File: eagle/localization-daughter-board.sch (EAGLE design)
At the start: 22 parts, among them J1 MOLEX-22-03-5035, U1 LM1085ISX-ADJ, U2 RPI-ZERO, U3 EXB-38V121JV, U4 TXS0101DCKR, U6 STM32F042FXP

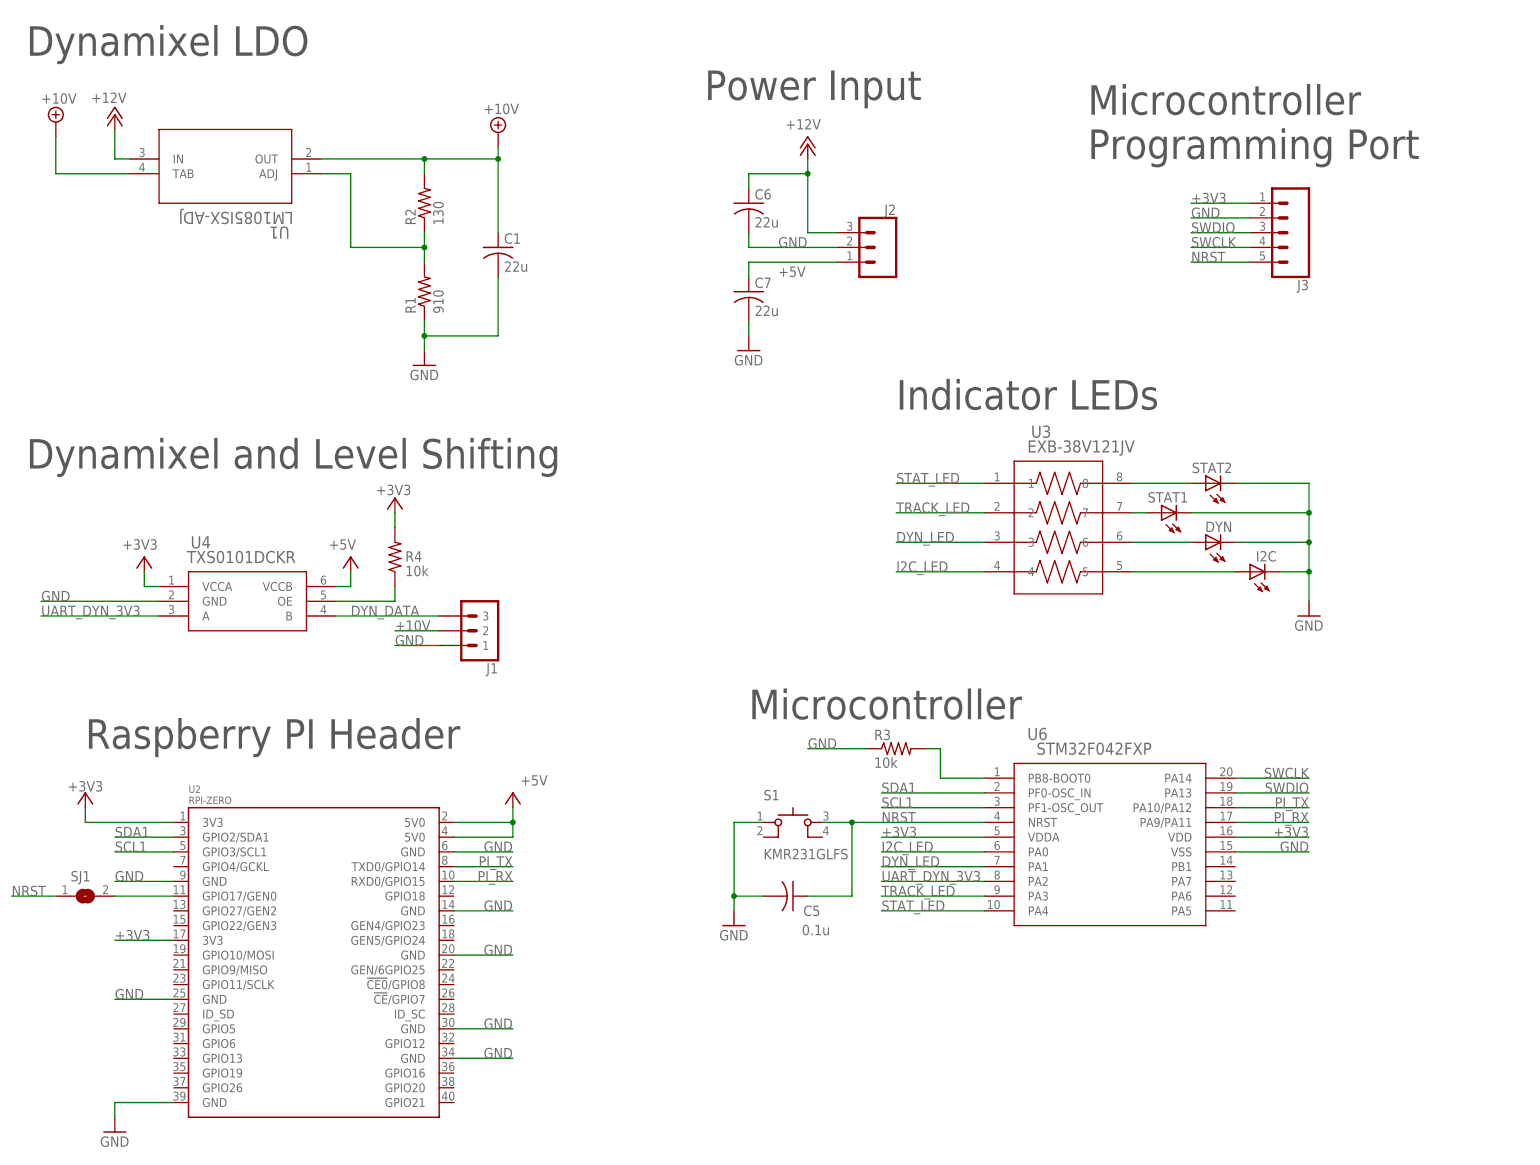
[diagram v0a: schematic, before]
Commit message: Broke out the rest of the micro pins. Adjusted the font on connectors
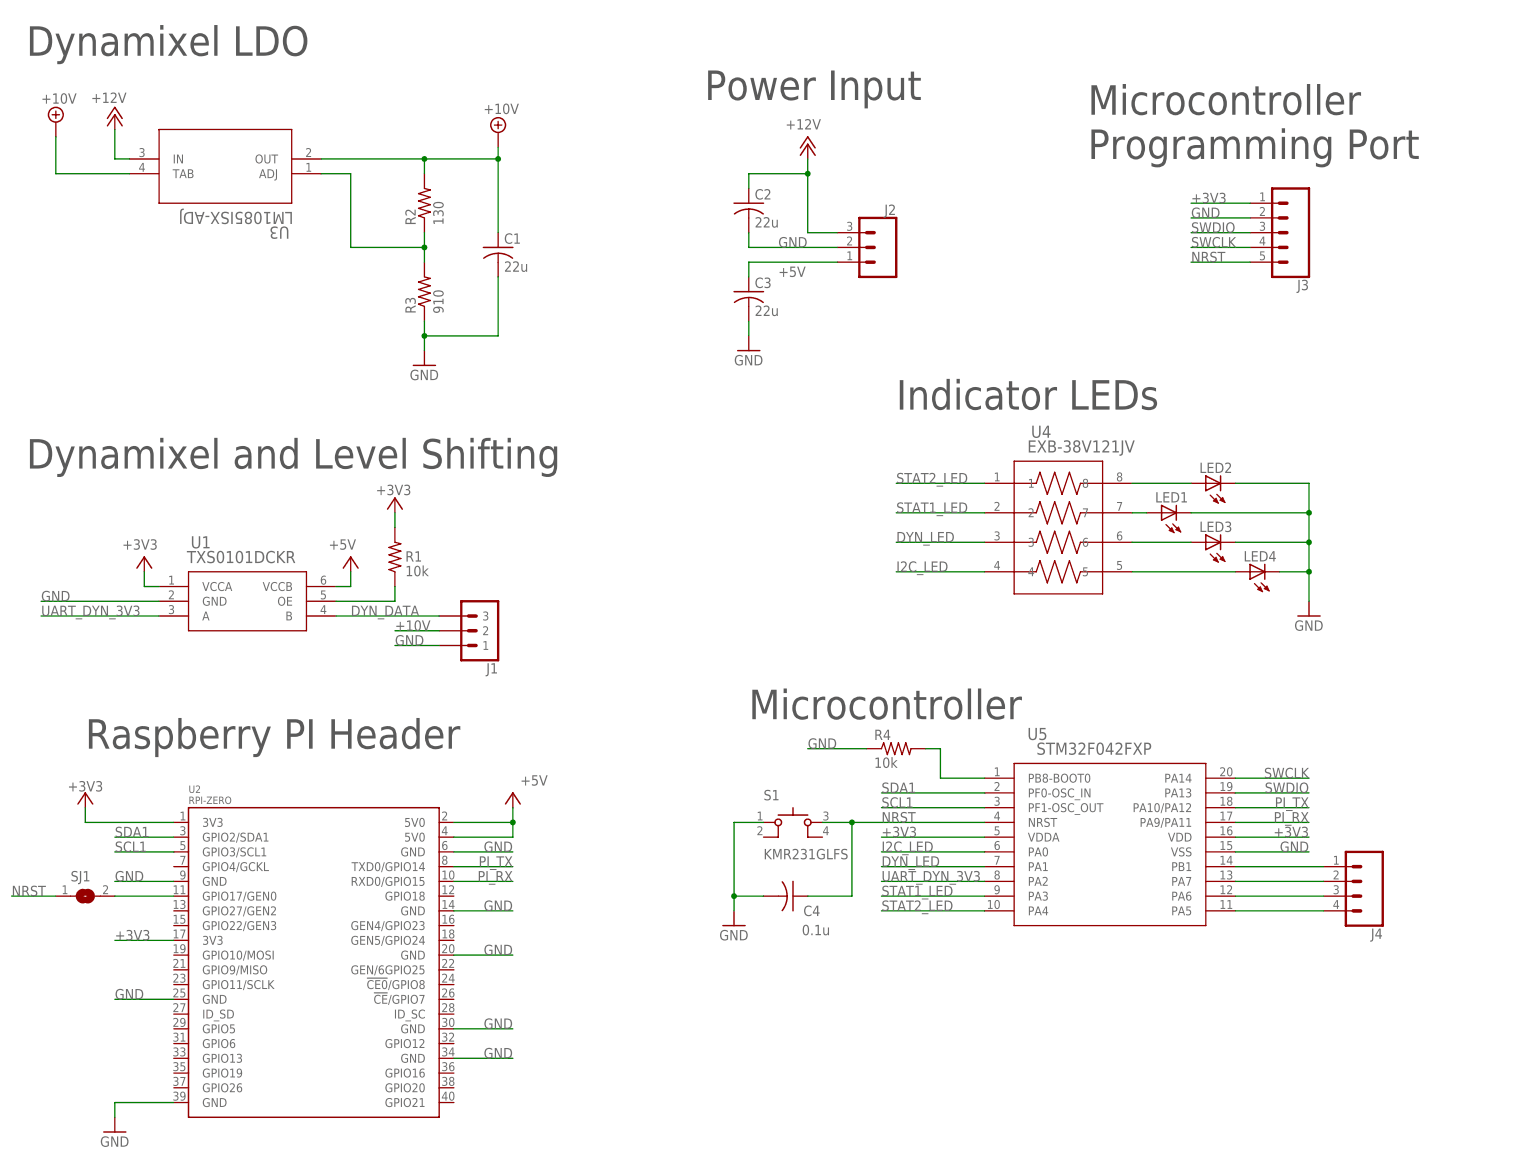
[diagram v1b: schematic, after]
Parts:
- added J4: (no value), SparkFun-Connectors:CONN_041X04_NO_SILK
- R1: value 910 -> 10k
- R3: value 10k -> 910
- U1: value LM1085ISX-ADJ -> TXS0101DCKR; device bbb_localization_cape:LM1085ISX-ADJ -> Localization-Daughter-Board:TXS0101DCKR
- U3: value EXB-38V121JV -> LM1085ISX-ADJ; device Localization-Daughter-Board:EXB-38V121JV -> bbb_localization_cape:LM1085ISX-ADJ
- U4: value TXS0101DCKR -> EXB-38V121JV; device Localization-Daughter-Board:TXS0101DCKR -> Localization-Daughter-Board:EXB-38V121JV
- renumbered C5 to C4, C6 to C2, C7 to C3, DYN to LED3, I2C to LED4, STAT1 to LED1, STAT2 to LED2, U6 to U5
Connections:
- removed net STAT_LED: U3.1, U5.PA4
- removed net TRACK_LED: U3.2, U5.PA3
- new net N$10: J4.4, U5.PA5
- new net N$7: J4.1, U5.PB1
- new net N$8: J4.2, U5.PA7
- new net N$9: J4.3, U5.PA6
- new net STAT1_LED: U4.2, U5.PA3
- new net STAT2_LED: U4.1, U5.PA4
- net +10V: now also U3.OUT, U3.TAB; no longer U1.OUT, U1.TAB
- net +12V: now also U3.IN; no longer U1.IN
- net +3V3: now also R1.2, U1.VCCA; no longer R4.2, U4.VCCA
- net +5V: now also U1.VCCB; no longer U4.VCCB
- net DYN_DATA: now also U1.B; no longer U4.B
- net DYN_LED: now also U4.3; no longer U3.3
- net DYN_OE: now also R1.1, U1.OE; no longer R4.1, U4.OE
- net GND: now also R4.1, U1.GND; no longer R1.1, U4.GND
- net I2C_LED: now also U4.4; no longer U3.4
- net N$1: now also R4.2; no longer R3.2
- net N$2: now also U4.7; no longer U3.7
- net N$3: now also R3.2, U3.ADJ; no longer R1.2, U1.ADJ
- net N$4: now also U4.6; no longer U3.6
- net N$5: now also U4.5; no longer U3.5
- net N$6: now also U4.8; no longer U3.8
- net UART_DYN_3V3: now also U1.A; no longer U4.A
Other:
- moved on the sheet: R1, R3, R4

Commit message: Current design
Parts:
- renumbered LED1 to STAT1, LED2 to STAT2, LED3 to DYN, LED4 to I2C

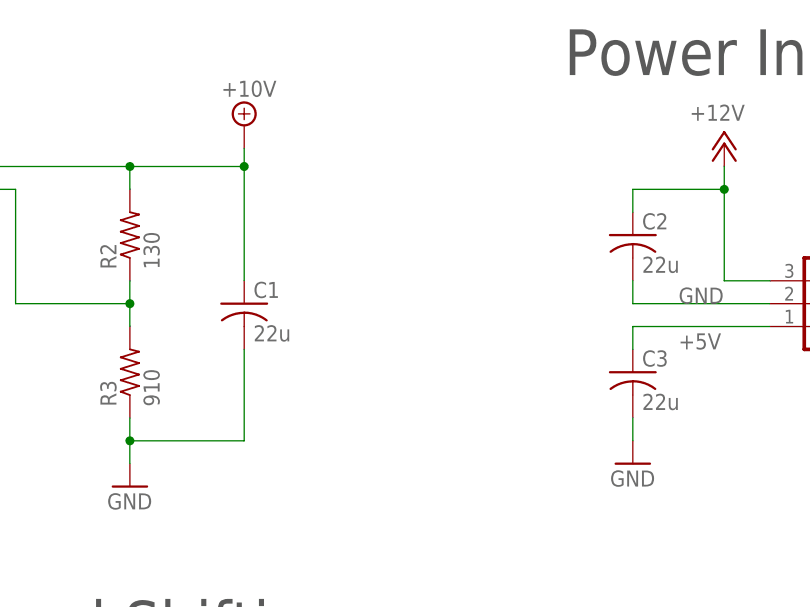
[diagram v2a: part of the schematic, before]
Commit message: Added additional capacitors
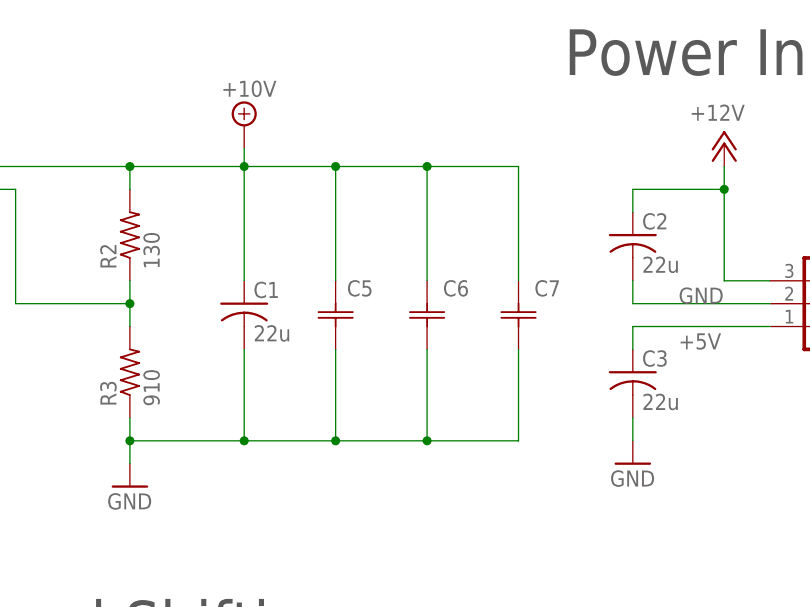
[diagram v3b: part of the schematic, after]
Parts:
- added C5, C6, C7: F931C107MCC, Localization-Daughter-Board:F931C107MCC
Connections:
- net +10V: now also C5.1, C6.1, C7.1
- net GND: now also C5.2, C6.2, C7.2
